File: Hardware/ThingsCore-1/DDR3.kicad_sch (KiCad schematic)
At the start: 27 parts, among them U2 K4B4G1646E-BYMA, U7 STM32MP133DAE7

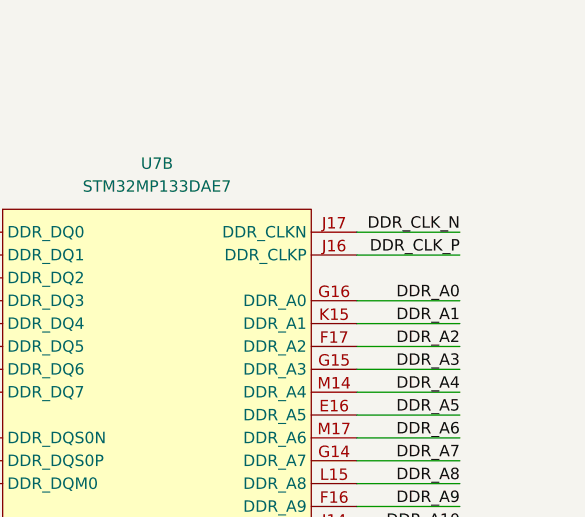
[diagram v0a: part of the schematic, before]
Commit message: ddr3 fanout done
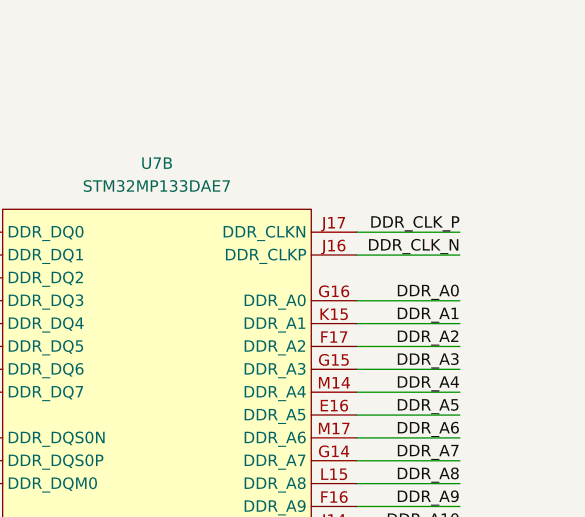
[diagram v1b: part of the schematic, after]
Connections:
- net DDR_CLK_N: now also U7.J16 (DDR_CLKP); no longer U7.J17 (DDR_CLKN)
- net DDR_CLK_P: now also U7.J17 (DDR_CLKN); no longer U7.J16 (DDR_CLKP)

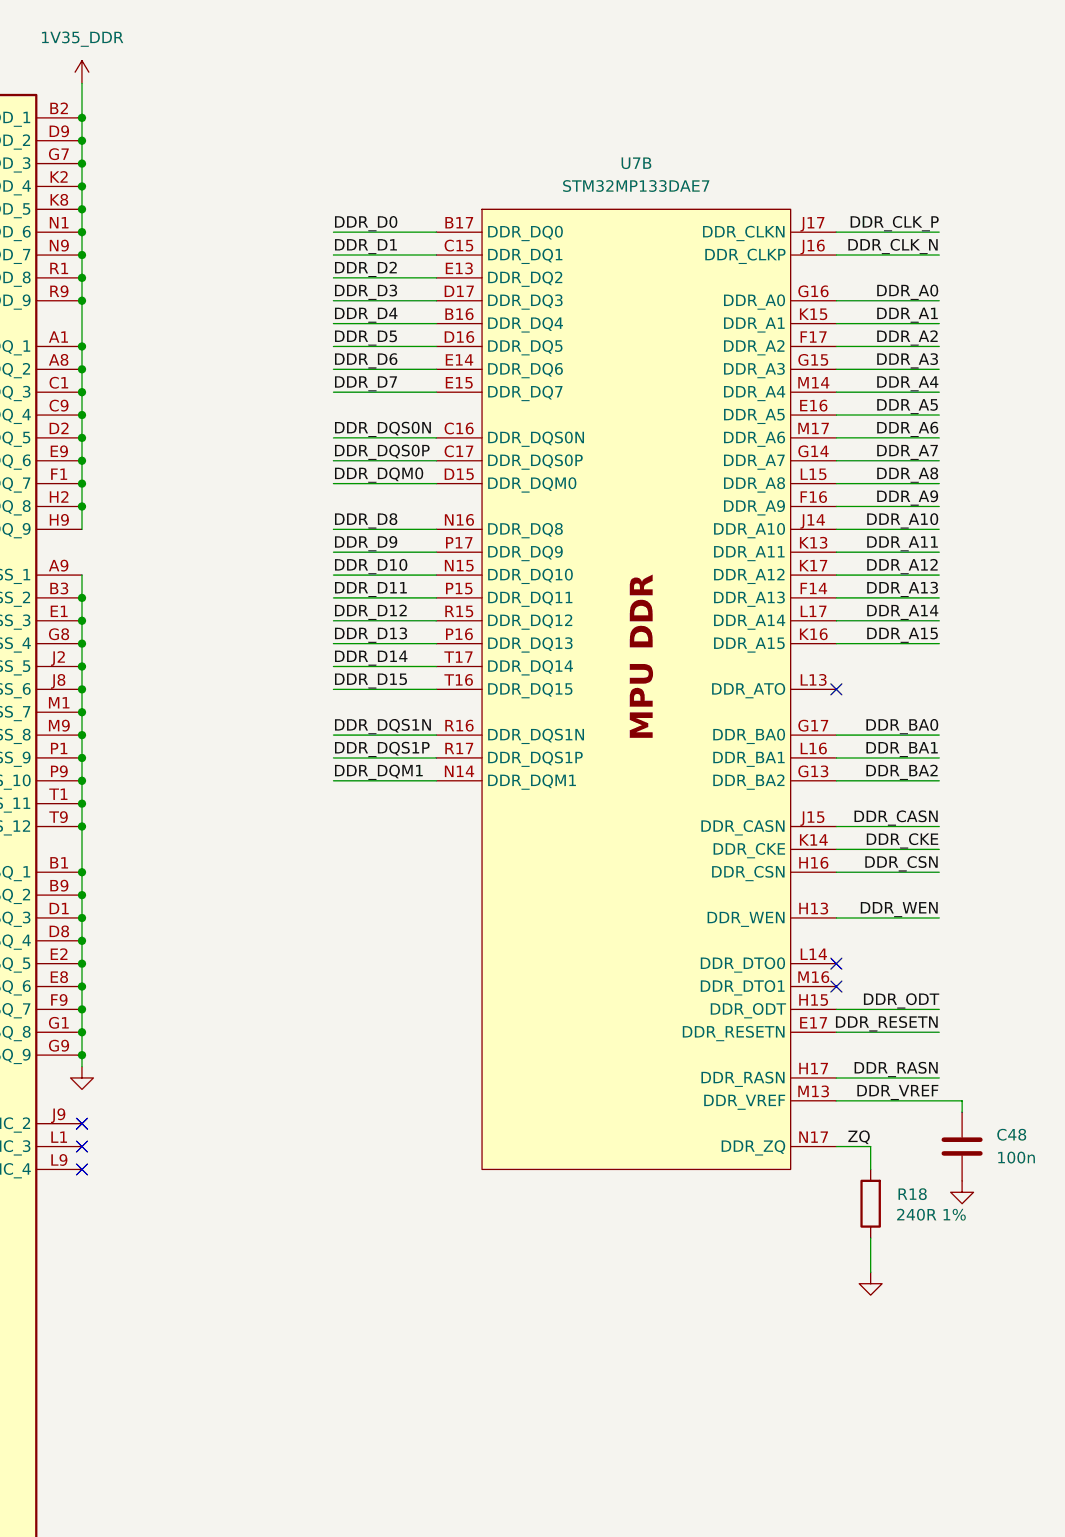
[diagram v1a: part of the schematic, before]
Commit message: pin assignment, rst,led, button pins left and checks
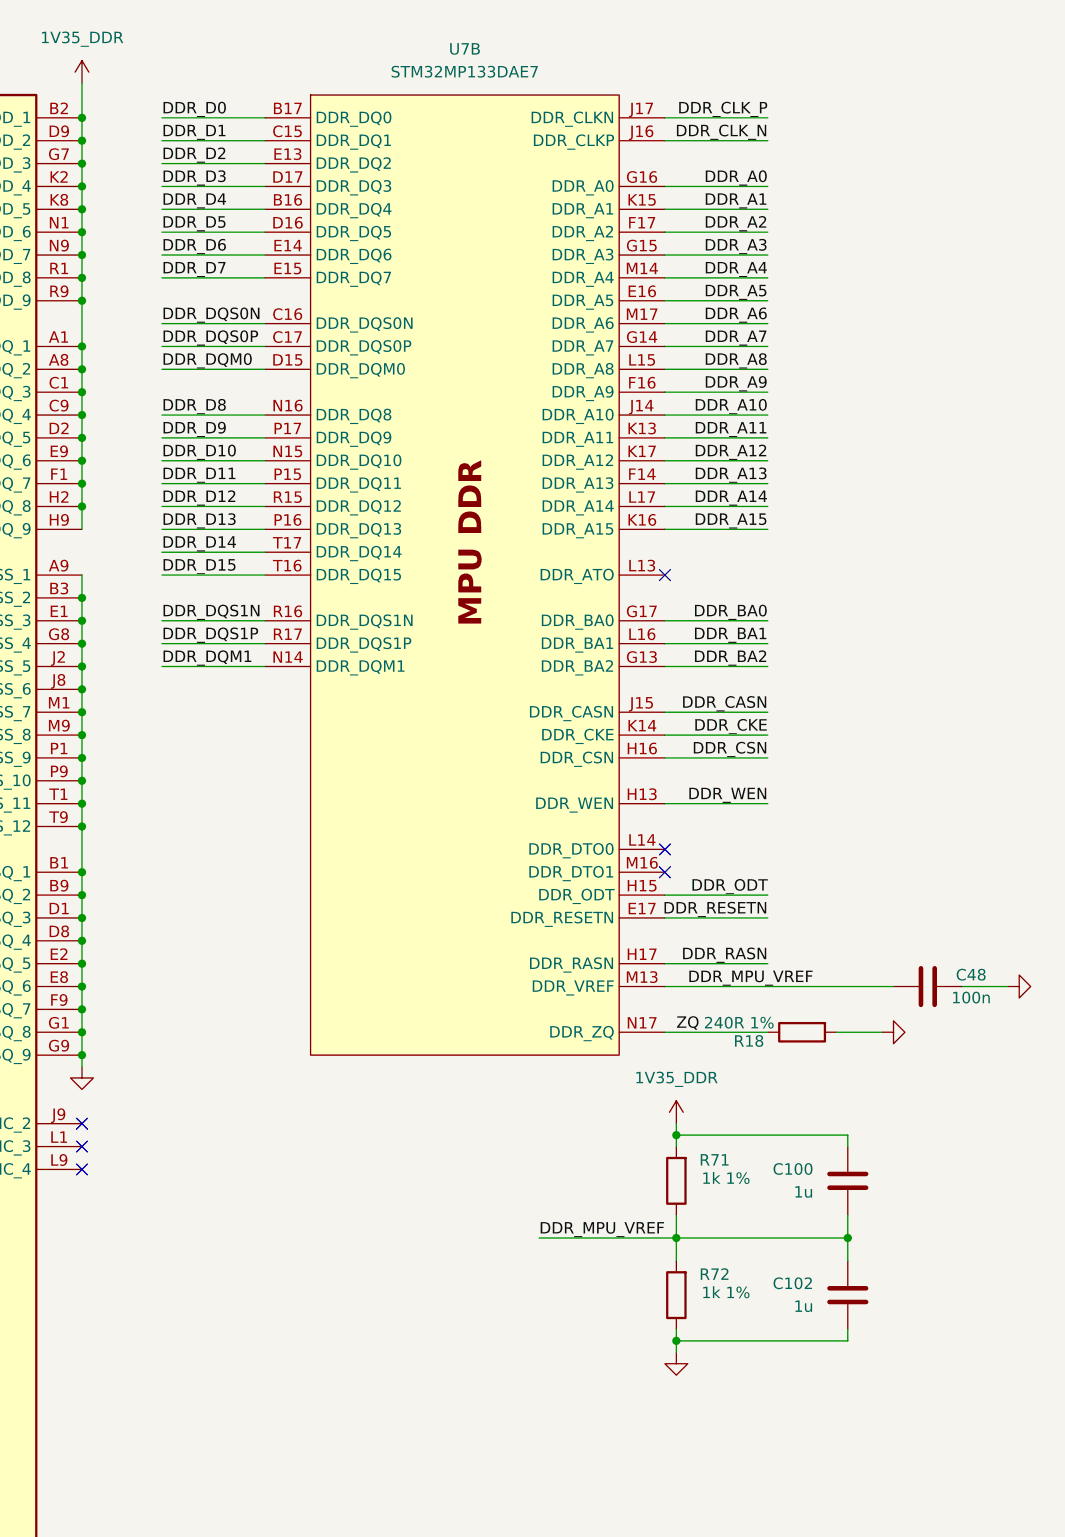
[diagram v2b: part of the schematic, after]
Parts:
- added C100, C102: 1u, Capacitor_SMD:C_0402_1005Metric, symbol Device:C
- added R71, R72: 1k 1%, Resistor_SMD:R_0402_1005Metric, symbol Device:R
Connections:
- net 1V35_DDR: now also C100.2, R71.2
- net DDR_VREF: no longer C48.2, U7.M13 (DDR_VREF)
- net GND: now also R18.2, C102.1, R72.1; no longer R18.1
- net ZQ: now also R18.1; no longer R18.2
- new net DDR_MPU_VREF: C100.1, C102.2, C48.2, R71.1, R72.2, U7.M13 (DDR_VREF)
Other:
- moved on the sheet: C48, R18, U7B
